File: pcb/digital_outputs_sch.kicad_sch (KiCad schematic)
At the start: 23 parts, among them CN2 VL0831510000G, K1 Relay_SPST-NO, K2 Relay_SPST-NO, K3 Relay_SPST-NO, K4 Relay_SPST-NO, Q1 BC807, Q2 BC807, Q3 BC807, Q4 BC807, U3 PCA8574D

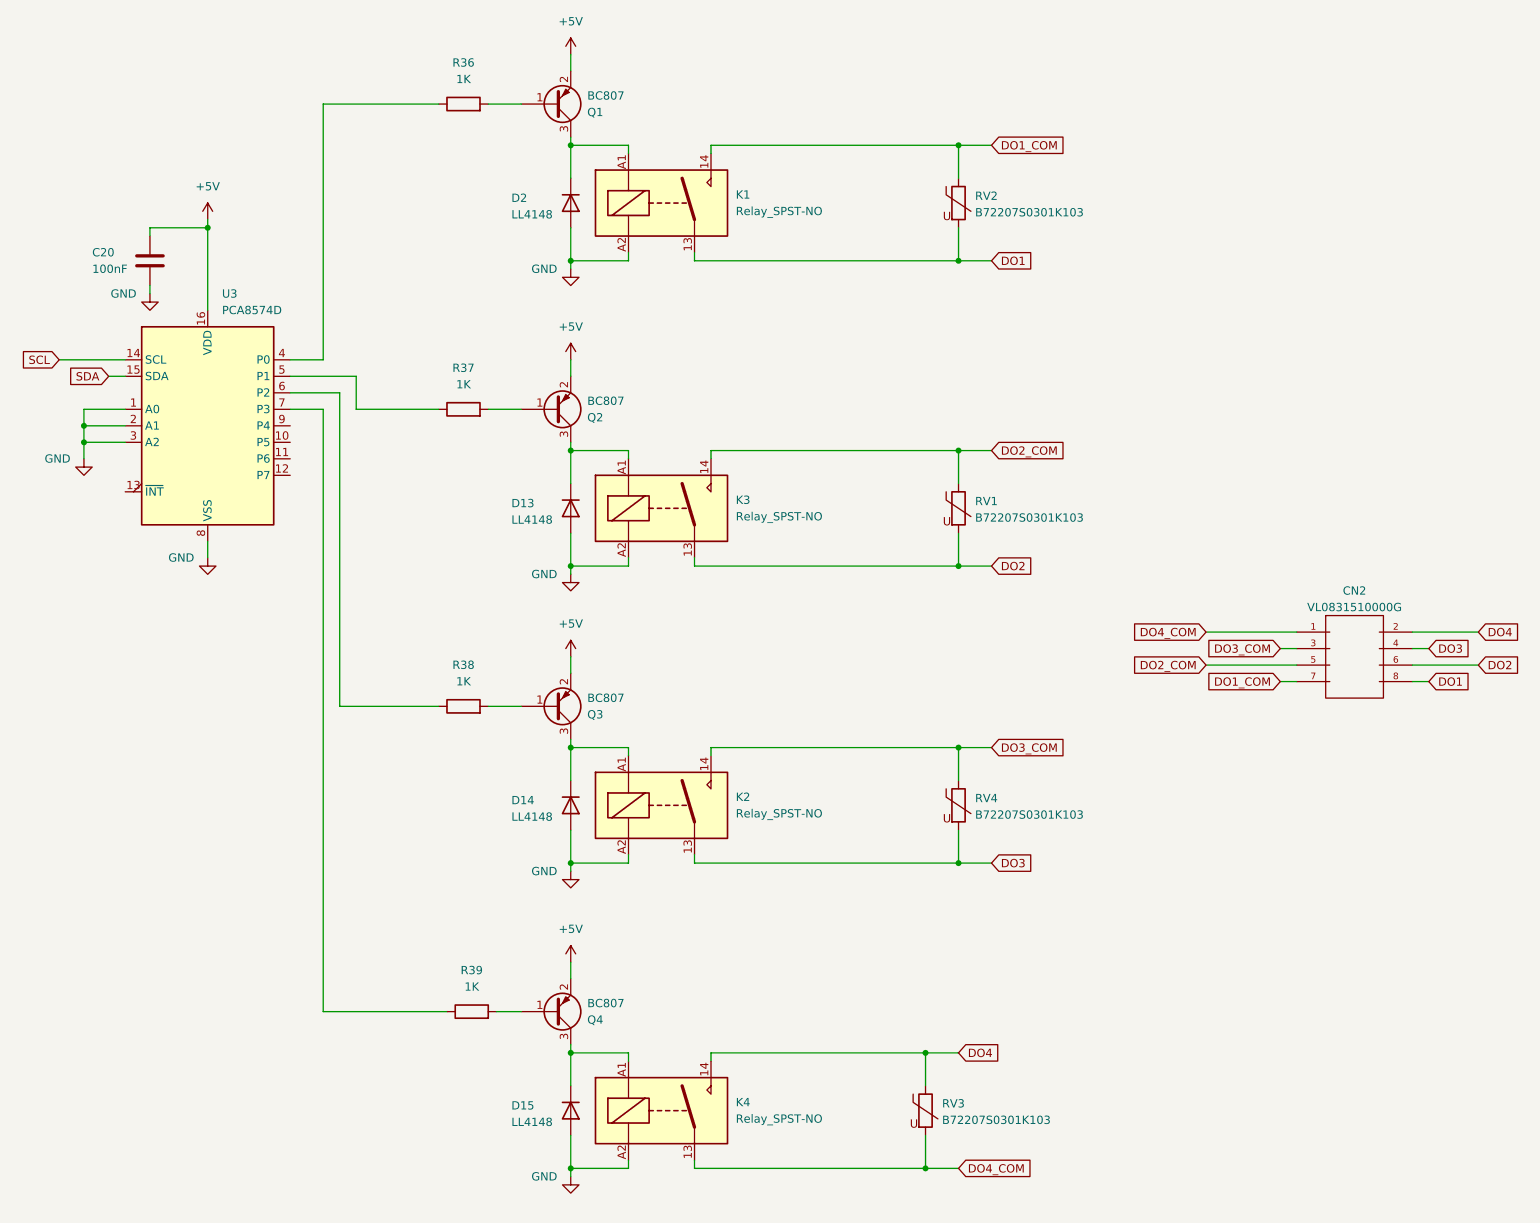
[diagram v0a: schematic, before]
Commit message: Minor changes in the digital outputs: changed 1K base resistors to 10K to save power. BC807 has an hfe of at least 100.
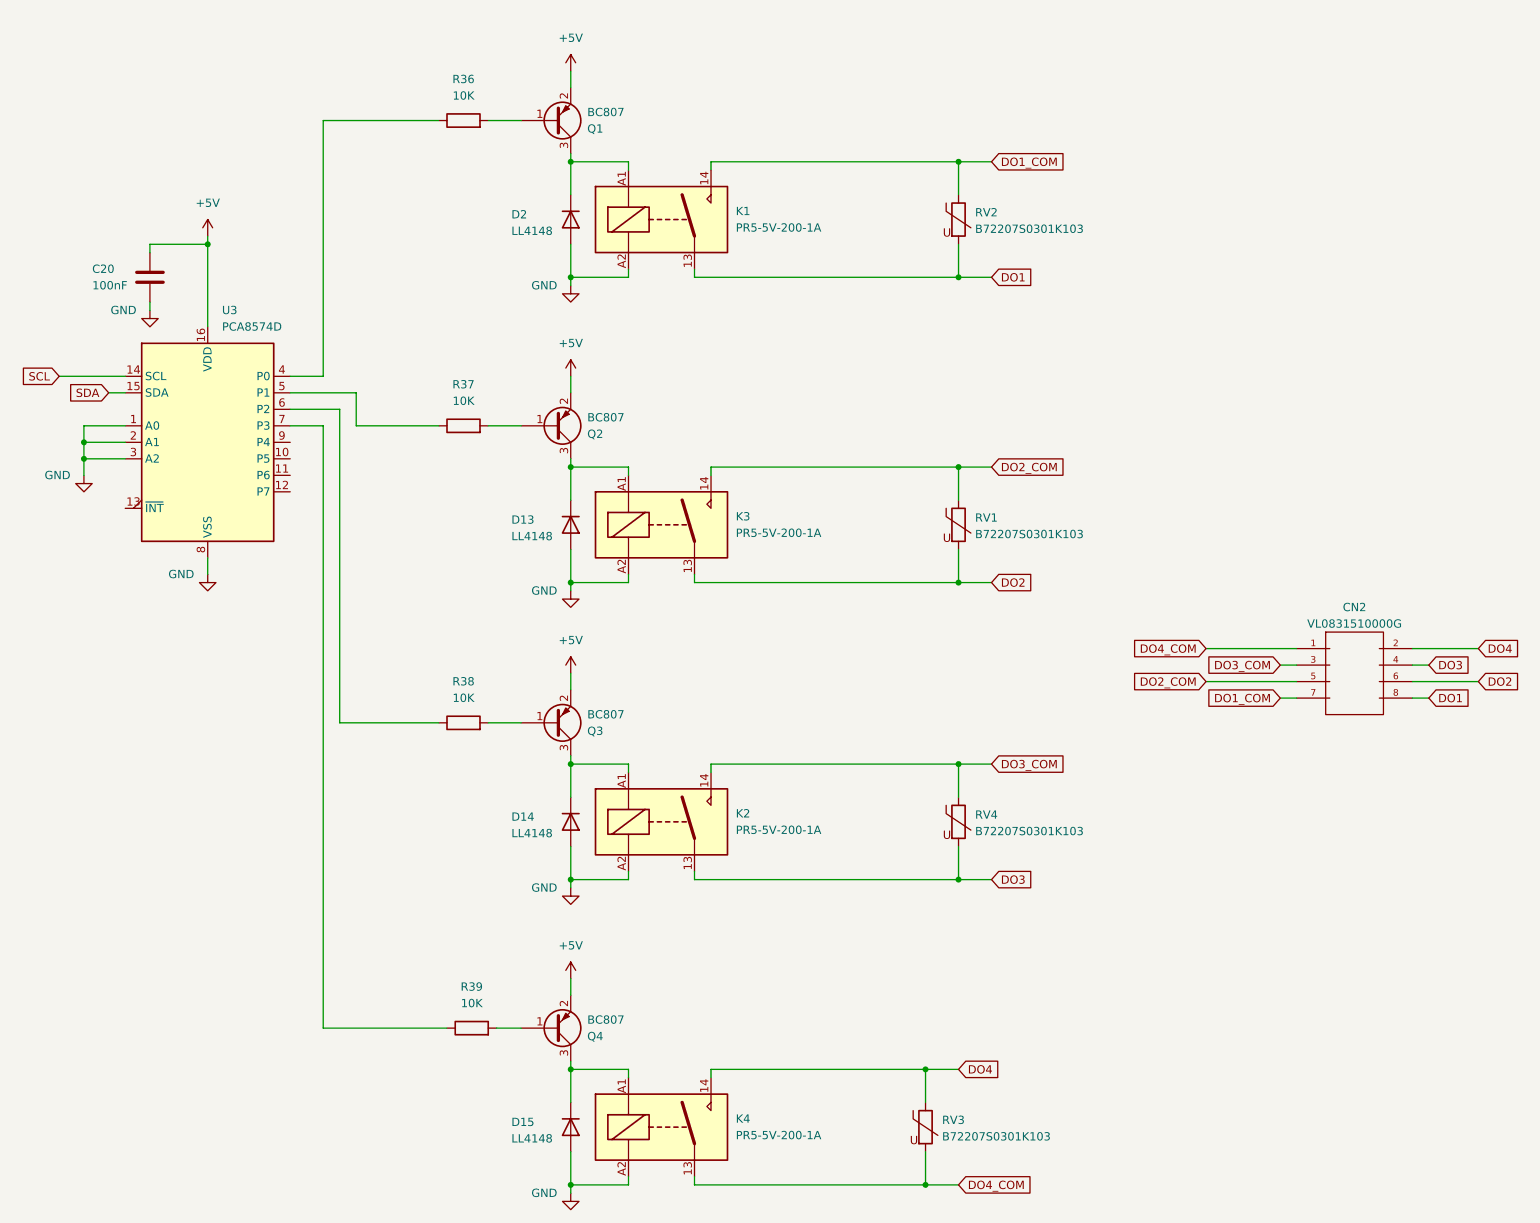
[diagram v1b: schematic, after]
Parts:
- K1, K2, K3, K4: value Relay_SPST-NO -> PR5-5V-200-1A
- R36, R37, R38, R39: value 1K -> 10K
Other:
- moved on the sheet: C20, CN2, D13, D14, D15, D2, K1, K2, K3, K4, Q1, Q2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
